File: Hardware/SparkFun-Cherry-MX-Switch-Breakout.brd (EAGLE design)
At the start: 19.1 x 19.1 mm, 20 parts

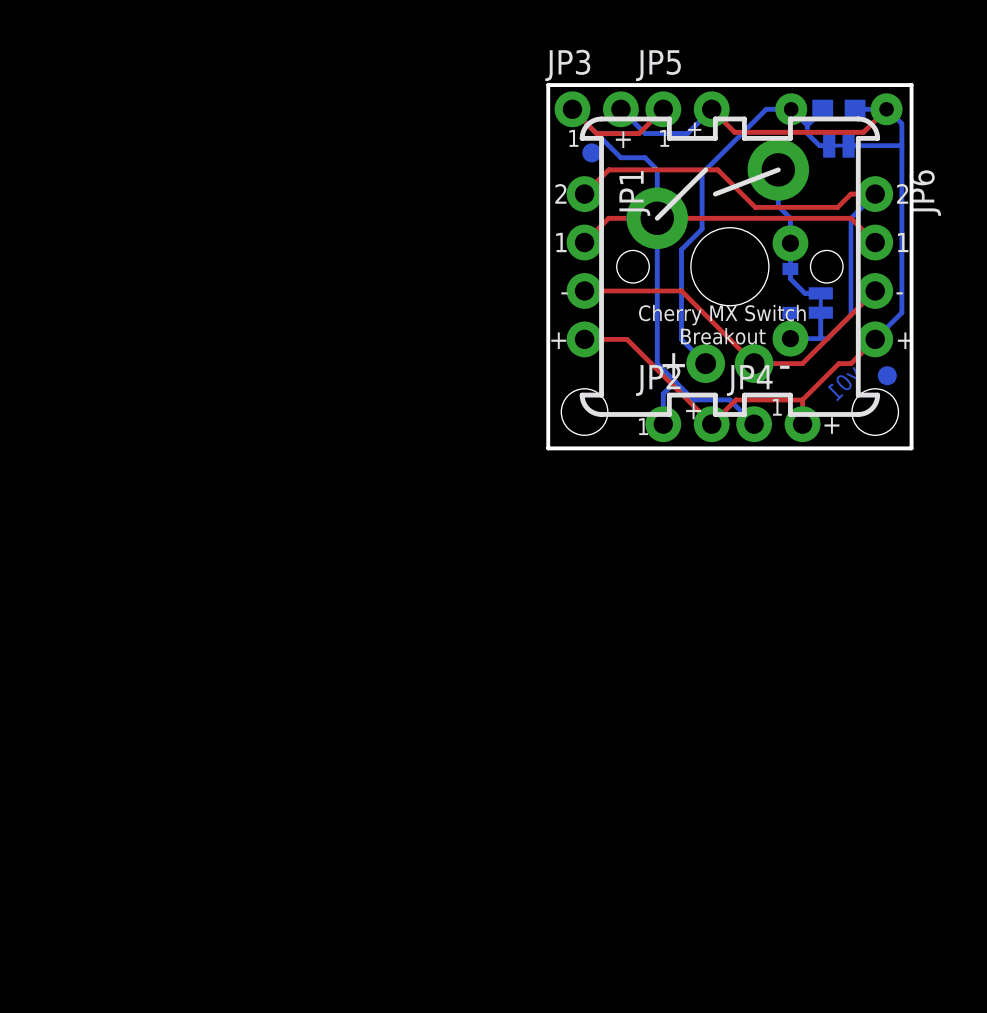
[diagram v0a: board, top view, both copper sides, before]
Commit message: Rearranging resistor and diode packages and standoffs.
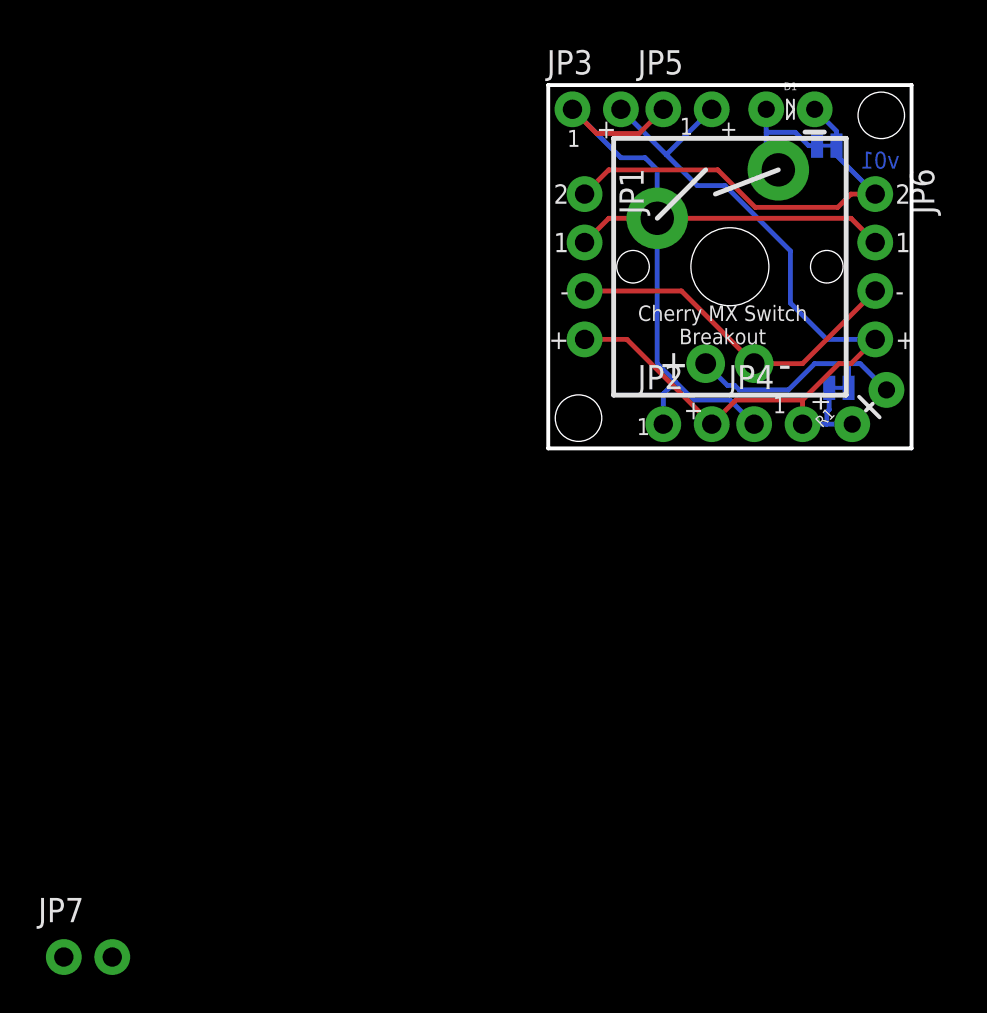
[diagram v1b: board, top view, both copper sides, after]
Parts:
- removed D2: (no value), cherry-temp:DIODE-1N4148-TIGHT
- removed FID1, FID2: FIDUCIAL1X2, SparkFun-Aesthetics:FIDUCIAL-1X2
- removed R2: (no value), SparkFun-Resistors:0603-RES
- added JP7: (no value), SparkFun-Connectors:1X02_NO_SILK
- D1: value (none) -> DNP; device SparkFun-DiscreteSemi:SOD-323 -> cherry-temp:DIODE-PTH-0.1
- R1: value (none) -> DNP; device SparkFun-Resistors:1/6W-RES -> SparkFun-Resistors:AXIAL-0.1
- moved R1 16.5 mm to (15.9, 1.27), flipped to the top, turned to 45 degrees
- moved STANDOFF1 15.6 mm to (17.5, 17.5)
- moved SJ1 12.7 mm to (15.2, 3.17), turned to 180 degrees
- moved D1 9.53 mm to (12.7, 17.8), flipped to the top, turned to 0 degrees
- moved SJ2 8.26 mm to (14.6, 15.9), turned to 180 degrees
- moved LOGO2 3.45 mm to (13.3, 9.65)
- moved STANDOFF2 0.45 mm to (1.59, 1.59)
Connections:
- net LEDA: now also R1.P$1; no longer R1.1, R2.1
- net N$1: now also R1.P$2; no longer R1.2, R2.2
- net N$3: no longer D2.A
- net SWITCH2: no longer D2.C
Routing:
- net N$1: track 21.2 -> 12.5 mm
- net SWITCH2: track 30.1 -> 22.6 mm
- net LEDA: track 53.6 -> 48.1 mm
- net N$3: track 7.88 -> 6.39 mm
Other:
- board text added: "D"
- board text added: "R"
- board text removed: "Dio"
- board text removed: "Res"
